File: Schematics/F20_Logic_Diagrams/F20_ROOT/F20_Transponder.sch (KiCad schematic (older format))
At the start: 1 part, among them U17 Transponder

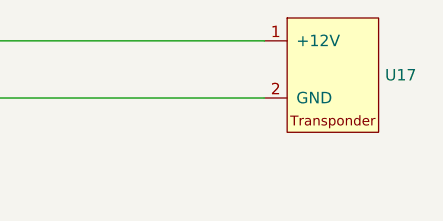
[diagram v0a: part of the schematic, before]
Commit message: Re-annotated Logic Diagrams, pulled a BOM list based on Logic Diagrams
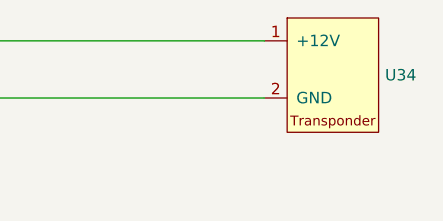
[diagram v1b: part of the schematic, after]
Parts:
- renumbered U17 to U34
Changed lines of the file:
@@
 $EndDescr
 $Comp
-L FSAE_Library:Transponder U17
+L FSAE_Library:Transponder U34
 U 1 1 5E38FBDA
 P 7500 3500
-F 0 "U17" H 8028 3350 50  0000 L CNN
+F 0 "U34" H 8028 3350 50  0000 L CNN
 F 1 "Transponder" H 7650 3550 50  0001 C CNN
 F 2 "" H 8000 4000 50  0001 C CNN
@@
 	3000 3750 3000 4000
 $Comp
-L FSAE_Library:GND #PWR015
+L FSAE_Library:GND #PWR018
 U 1 1 5E3B8D8B
 P 3000 4000
-F 0 "#PWR015" H 3000 3800 50  0001 C CNN
+F 0 "#PWR018" H 3000 3800 50  0001 C CNN
 F 1 "GND" H 3004 3846 50  0000 C CNN
 F 2 "" H 3000 3950 50  0001 C CNN
